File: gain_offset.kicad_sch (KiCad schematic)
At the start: 3 parts, among them U3 AD628, U4 ADA4938-1, U5 ADC128D818

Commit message: First schematic version of AF
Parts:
- removed U3: AD628, symbol Amplifier_Difference:AD628
- removed U4: ADA4938-1, Package_CSP:LFCSP-16-1EP_3x3mm_P0.5mm_EP1.3x1.3mm_ThermalVias, symbol Amplifier_Difference:ADA4938-1
- removed U5: ADC128D818, Package_SO:TSSOP-16_4.4x5mm_P0.65mm, symbol Analog_ADC:ADC128D818
- added C11, C12, C13, C14: C, symbol Device:C
- added R17, R18, R19, R20, R21, R22, R23, R24, R25, R26, R27, R4, R5, R6, R7: R, symbol Device:R
- added U2: LTC6754xSC6, Package_TO_SOT_SMD:SOT-363_SC-70-6, symbol Comparator:LTC6754xSC6
- added U3, U5: AD8337BCPZ-REEL-ND, CP_8_2_ADI, symbol 2025-07-13_23-24-37:AD8337BCPZ-REEL-ND
- added U4, U7: LMH6551MA, Package_SO:SOIC-8_3.9x4.9mm_P1.27mm, symbol Amplifier_Operational:LMH6551MA
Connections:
- new net: R22.2, R27.1, U4.4 (+)
- new net: R19.1, R27.2, U4.1 (-)
- new net: R17.2, R5.2, R6.1, U7.5 (-)
- new net: R18.1, R26.2, U4.8 (+)
- new net: R20.2, R21.2, R26.1, U4.5 (-)
- new net: R25.1, R6.2, U7.8 (+)
- new net: R24.1, R7.2, U7.1 (-)
- new net: R4.2, R7.1, U7.4 (+)
- new net: R23.1, U2.3 (+)
- new net AN_TRIGGER: R17.1, R20.1, U2.4 (-)
- new net AN_TRIGGER_N: U2.6 (~{Q})
- new net AN_TRIGGER_P: U2.1 (Q)
- new net CH1_CH+: C11.2, C12.2, R22.1, R4.1
- new net CH1_CH-: C11.1, C12.1, R21.1, R5.1
- new net CH1_COMMON: C13.1, U7.2 (VCM)
- new net CH1_OFFSET: R24.2
- new net CH2_COMMON: C14.1, U4.2 (VCM)
- new net CH2_OFFSET: R19.2
- new net GND: C13.2, C14.2
- new net TRIGGER_LEVEL: R23.2
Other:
- note removed: "ADC driver"
- note removed: "Gain"
- note removed: "adc"

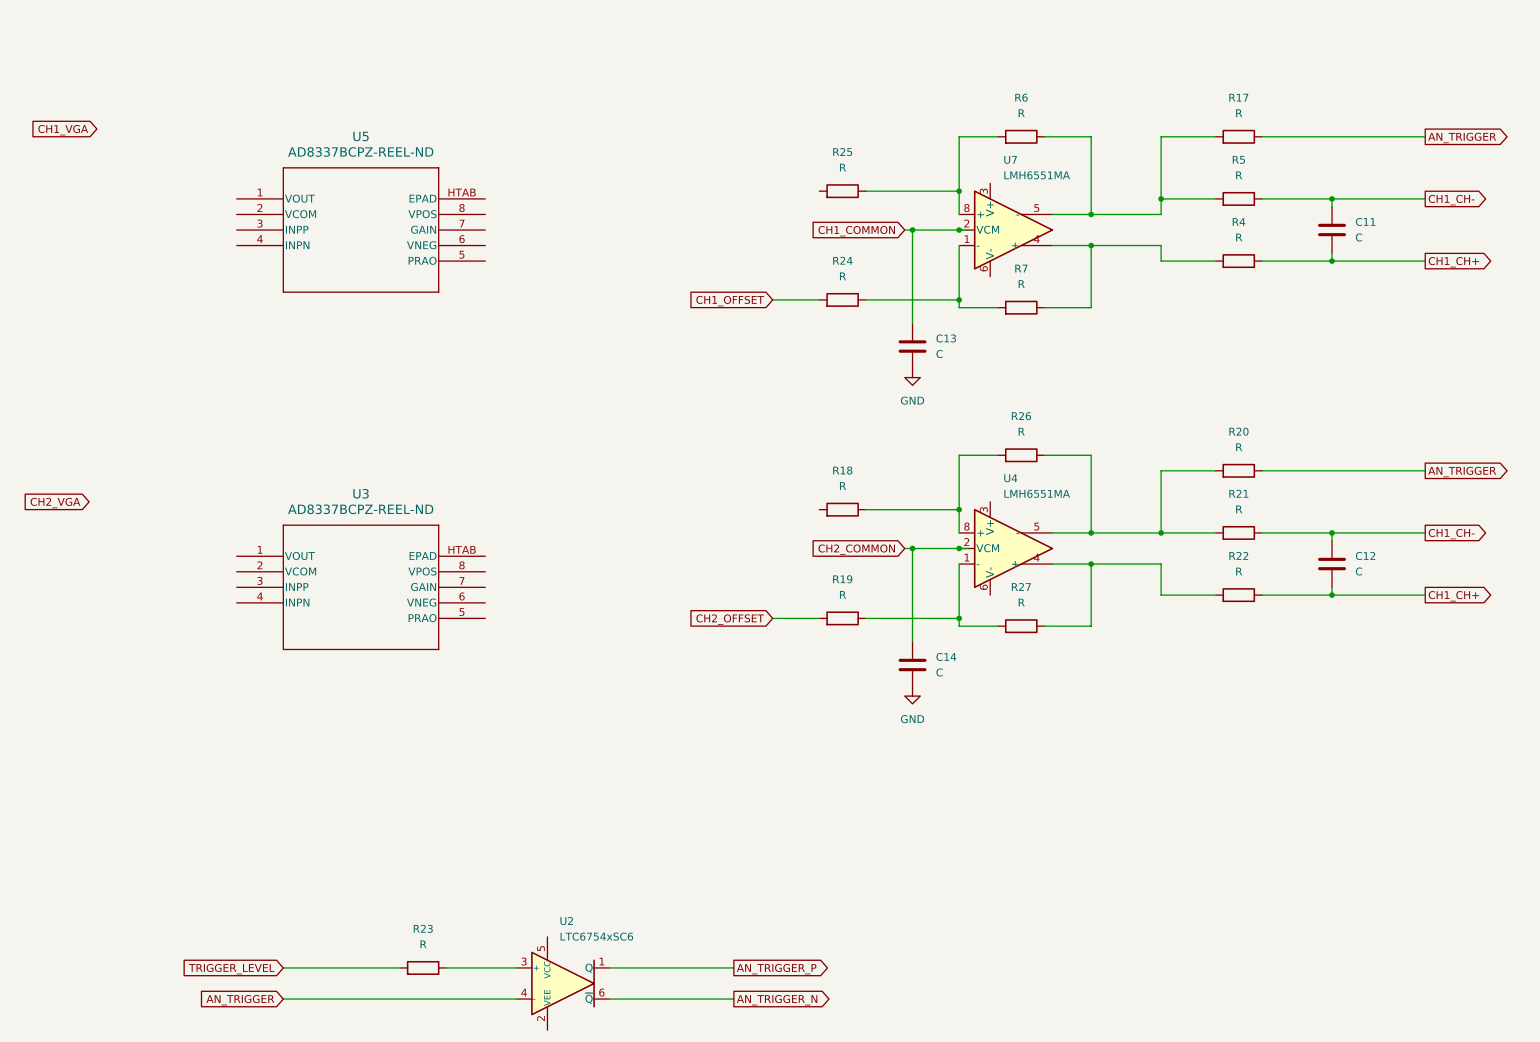
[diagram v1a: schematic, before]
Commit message: Chose amplifiers
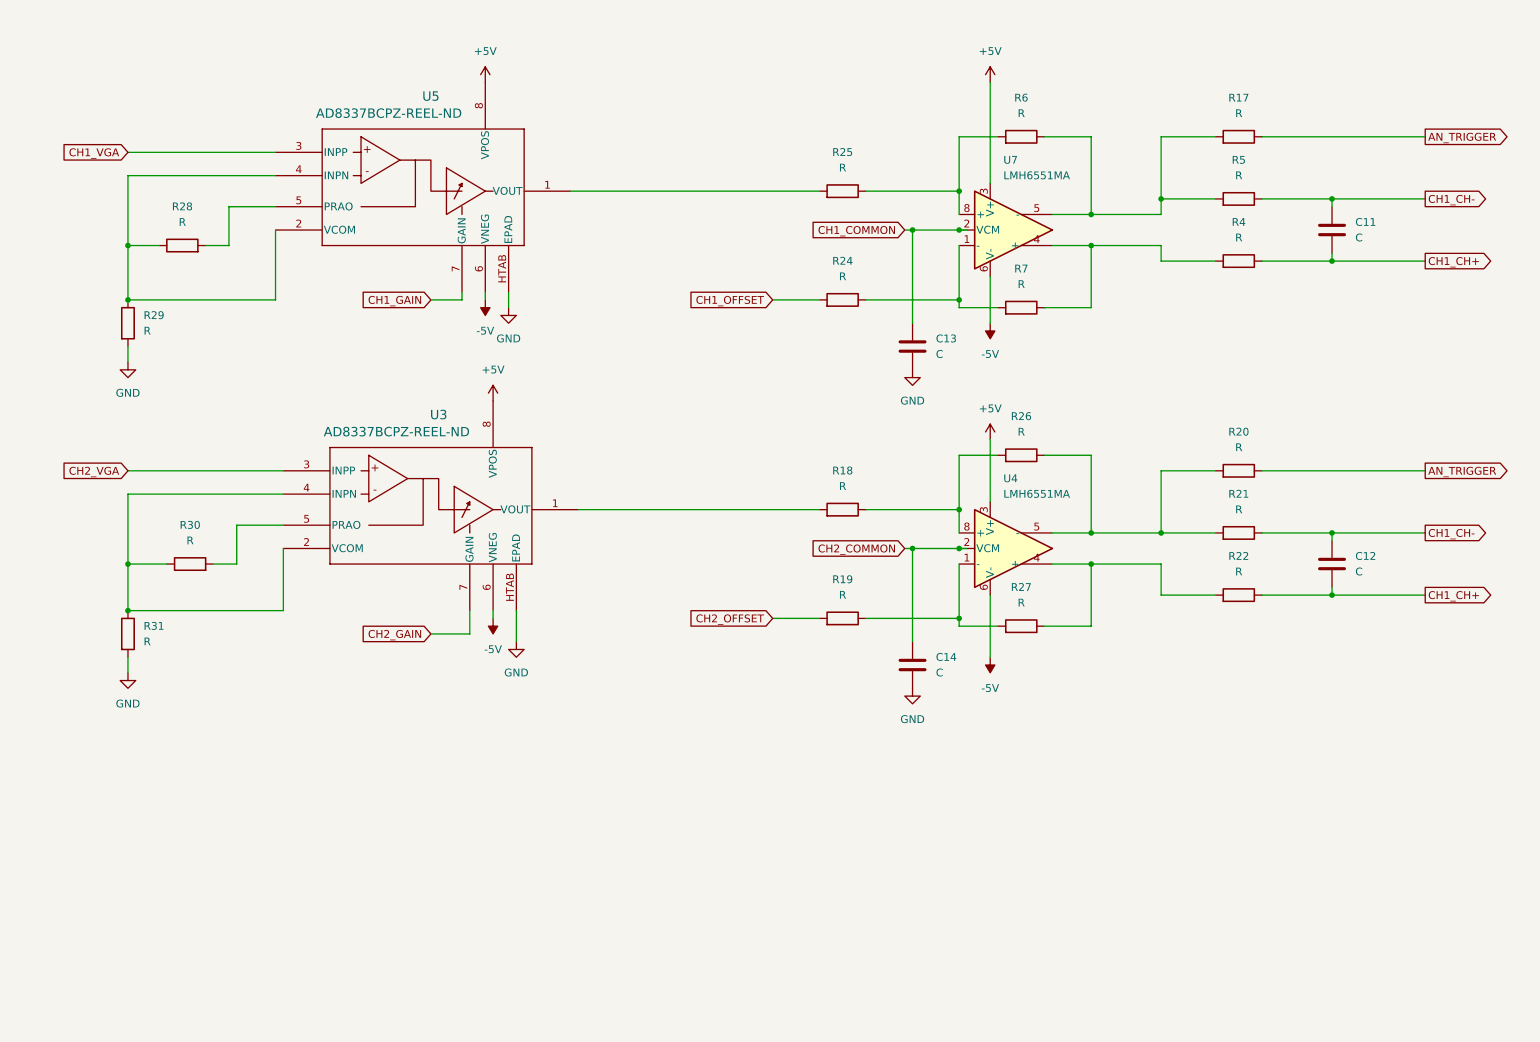
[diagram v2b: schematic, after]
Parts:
- removed R23: R, symbol Device:R
- removed U2: LTC6754xSC6, Package_TO_SOT_SMD:SOT-363_SC-70-6, symbol Comparator:LTC6754xSC6
- added R28, R29, R30, R31: R, symbol Device:R
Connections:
- net CH1_VGA: now also U5.3 (INPP)
- net CH2_VGA: now also U3.3 (INPP)
- net GND: now also U3.HTAB (EPAD), U5.HTAB (EPAD), R29.2, R31.2
- net at U5.1 (VOUT): now also R25.2
- net at U5.2 (VCOM): now also U5.4 (INPN), R28.1, R29.1
- net at U5.5 (PRAO): now also R28.2
- net -5V: now reaches U5.6 (VNEG)
- net -5V: now also U3.6 (VNEG), U4.6 (V-), U7.6 (V-)
- net CH1_GAIN: now reaches U5.7 (GAIN)
- net +5V: now reaches U5.8 (VPOS)
- net +5V: now also U3.8 (VPOS), U4.3 (V+), U7.3 (V+)
- net at R18.2: now also U3.1 (VOUT)
- net at U3.2 (VCOM): now also U3.4 (INPN), R30.1, R31.1
- net at U3.5 (PRAO): now also R30.2
- net CH2_GAIN: now reaches U3.7 (GAIN)

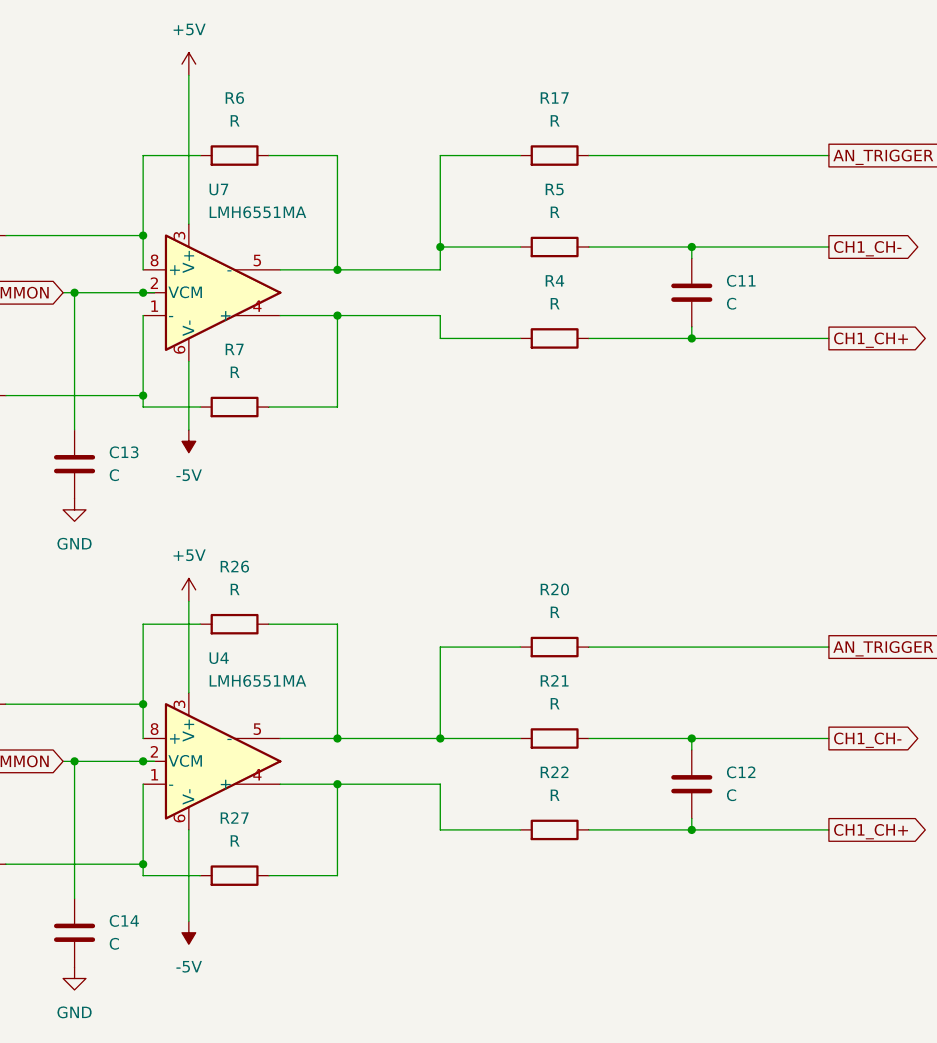
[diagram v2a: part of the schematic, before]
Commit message: Add some of the AF power supply levels
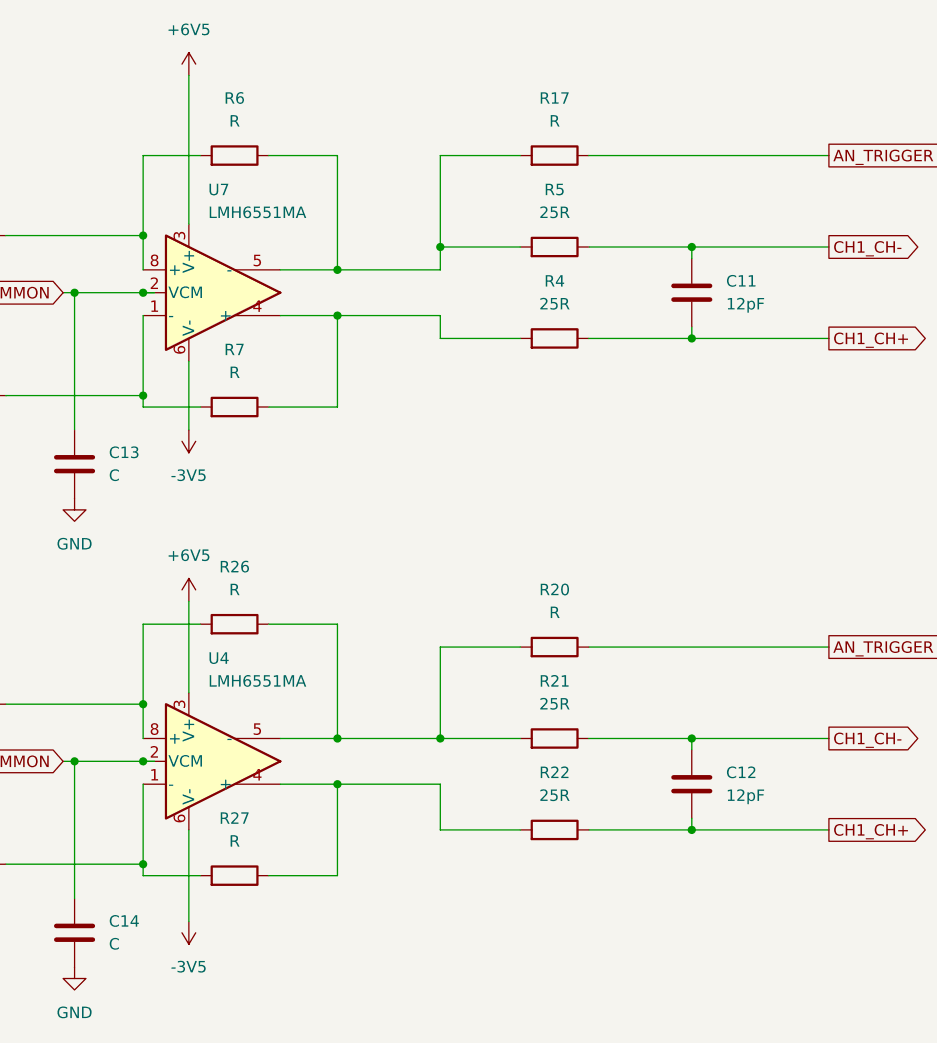
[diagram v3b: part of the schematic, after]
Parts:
- C11, C12: value C -> 12pF
- R21, R22, R4, R5: value R -> 25R
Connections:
- net +5V: no longer U4.3 (V+), U7.3 (V+)
- net -5V: no longer U4.6 (V-), U7.6 (V-)
- new net +6V5: U4.3 (V+), U7.3 (V+)
- new net -3V5: U4.6 (V-), U7.6 (V-)

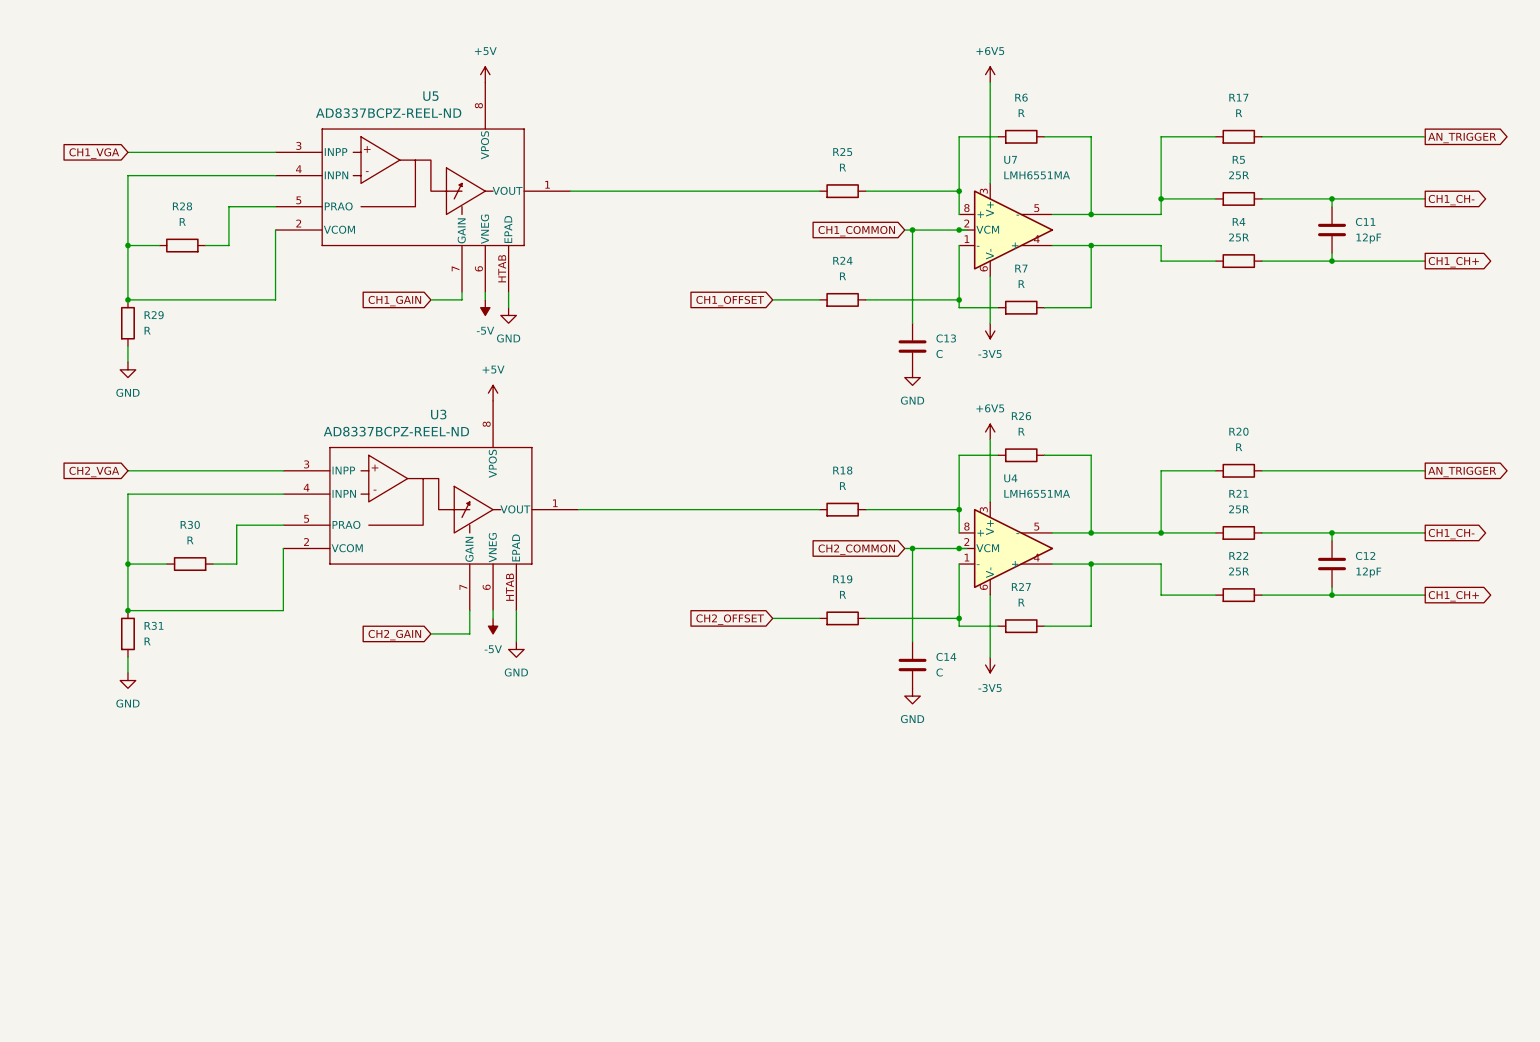
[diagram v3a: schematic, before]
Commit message: Move the trigger
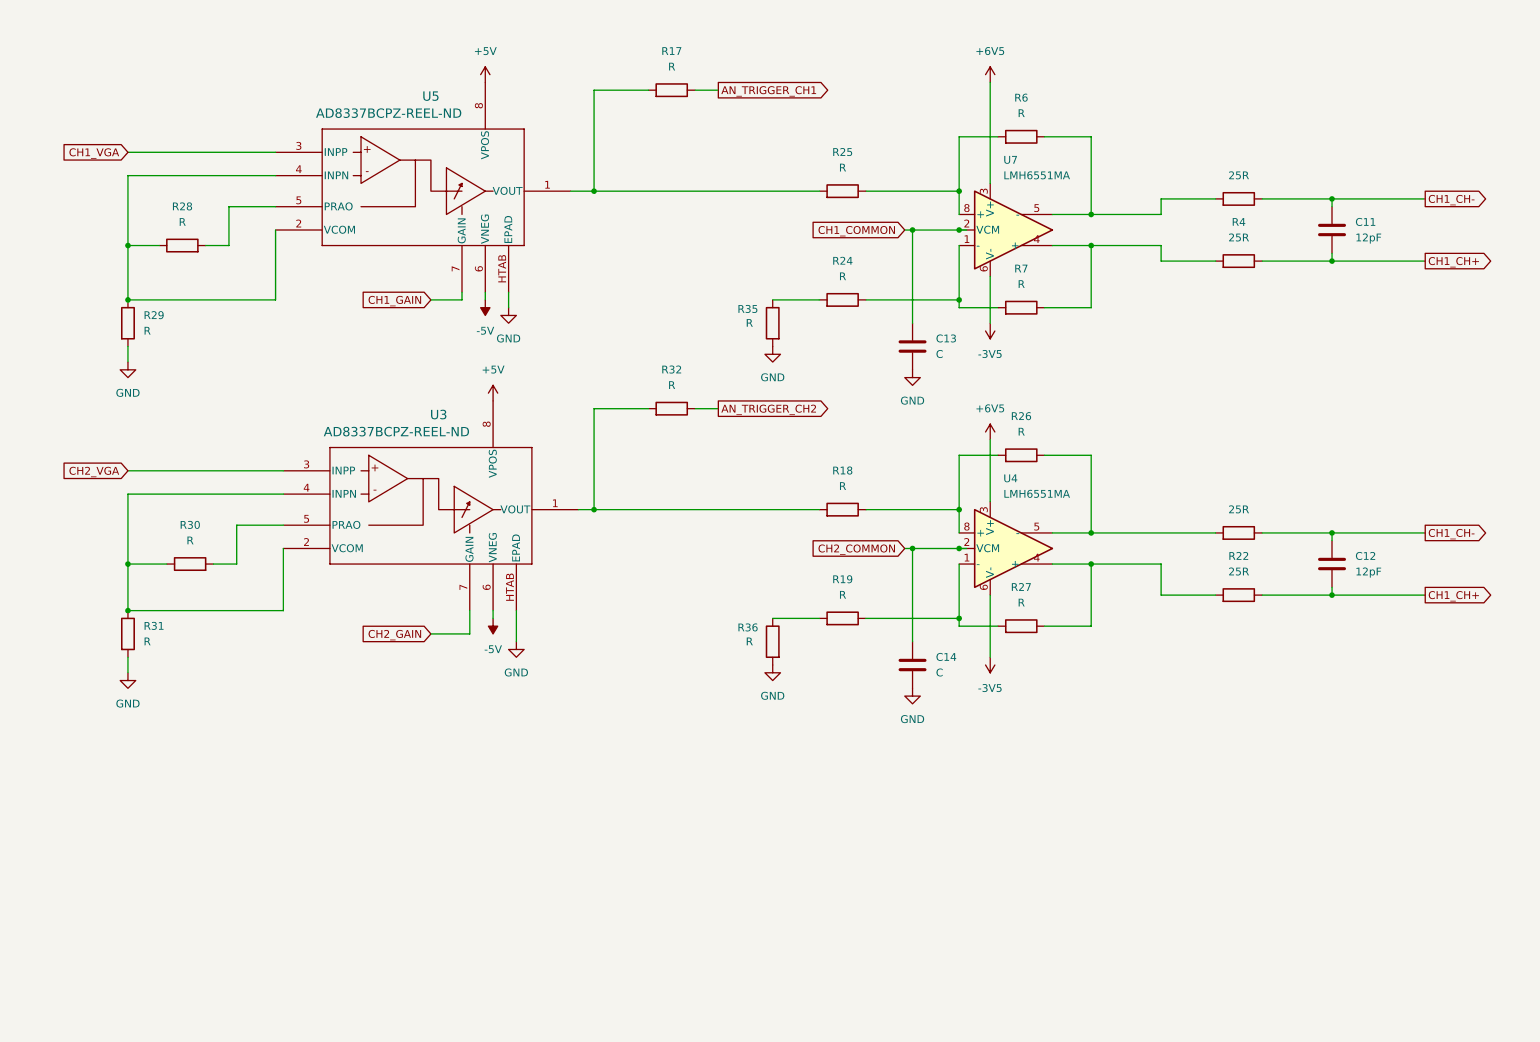
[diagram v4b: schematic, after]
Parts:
- removed R20: R, symbol Device:R
- added R32, R35, R36: R, symbol Device:R
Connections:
- net GND: now also R35.2, R36.2
- net at R25.2, U5.1 (VOUT): now also R17.2
- net at R5.2, R6.1, U7.5 (-): no longer R17.2
- net at R18.2, U3.1 (VOUT): now also R32.2
- net AN_TRIGGER renamed AN_TRIGGER_CH1
- net CH1_OFFSET: no longer names the net of R24.2
- net CH1_OFFSET: now also R35.1
- net CH2_OFFSET: no longer names the net of R19.2
- net CH2_OFFSET: now also R36.1
- new net AN_TRIGGER_CH2: R32.1
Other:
- moved on the sheet: R17
